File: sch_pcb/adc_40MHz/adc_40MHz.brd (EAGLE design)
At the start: 99 x 54.3 mm, 63 parts, among them IC1 LTC2227, IC2 LT6600-15, IC3 LTC6254XMS, IC5 LT1521XST, X1 SIGNAL, X2 CLK

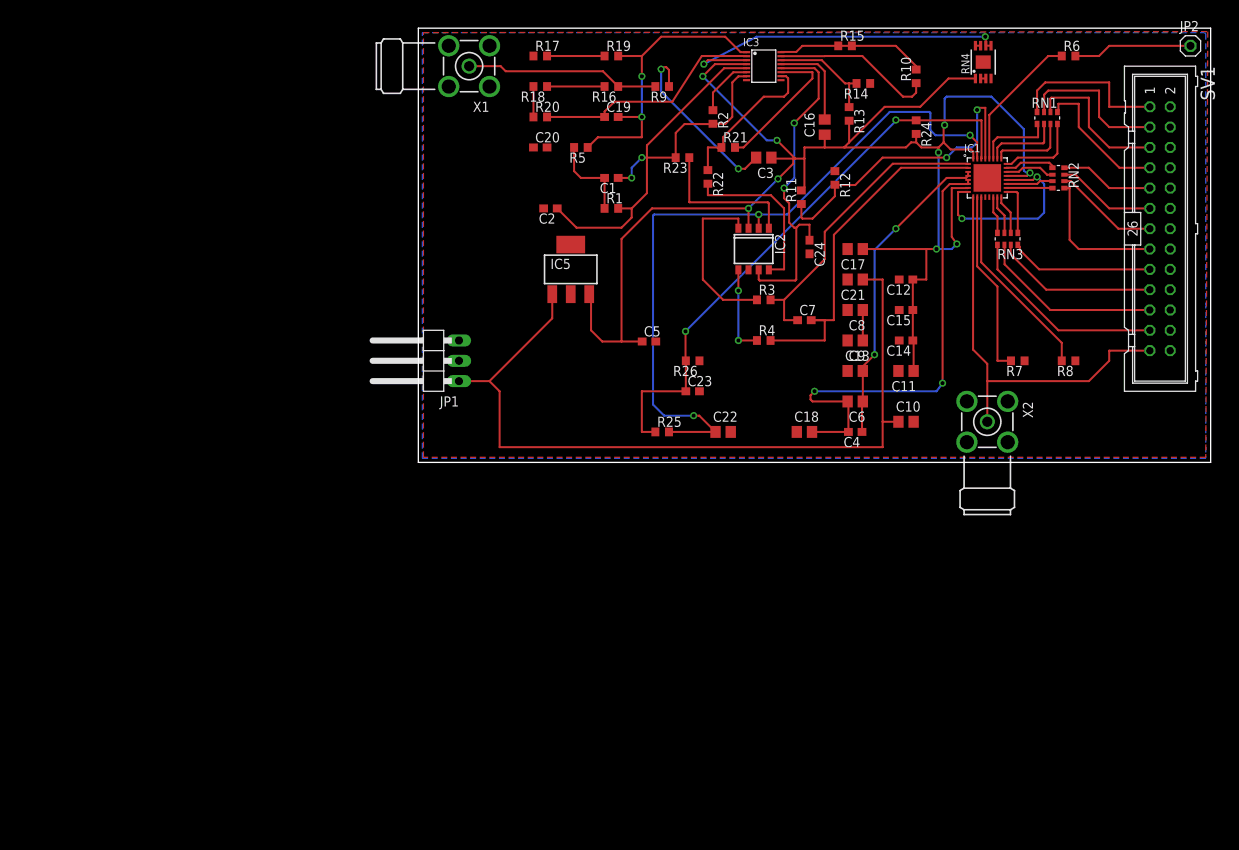
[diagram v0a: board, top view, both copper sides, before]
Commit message: Dokonczono model inwertera. Dodano go na schemat. Przed zmiana przetwornika na AD9235
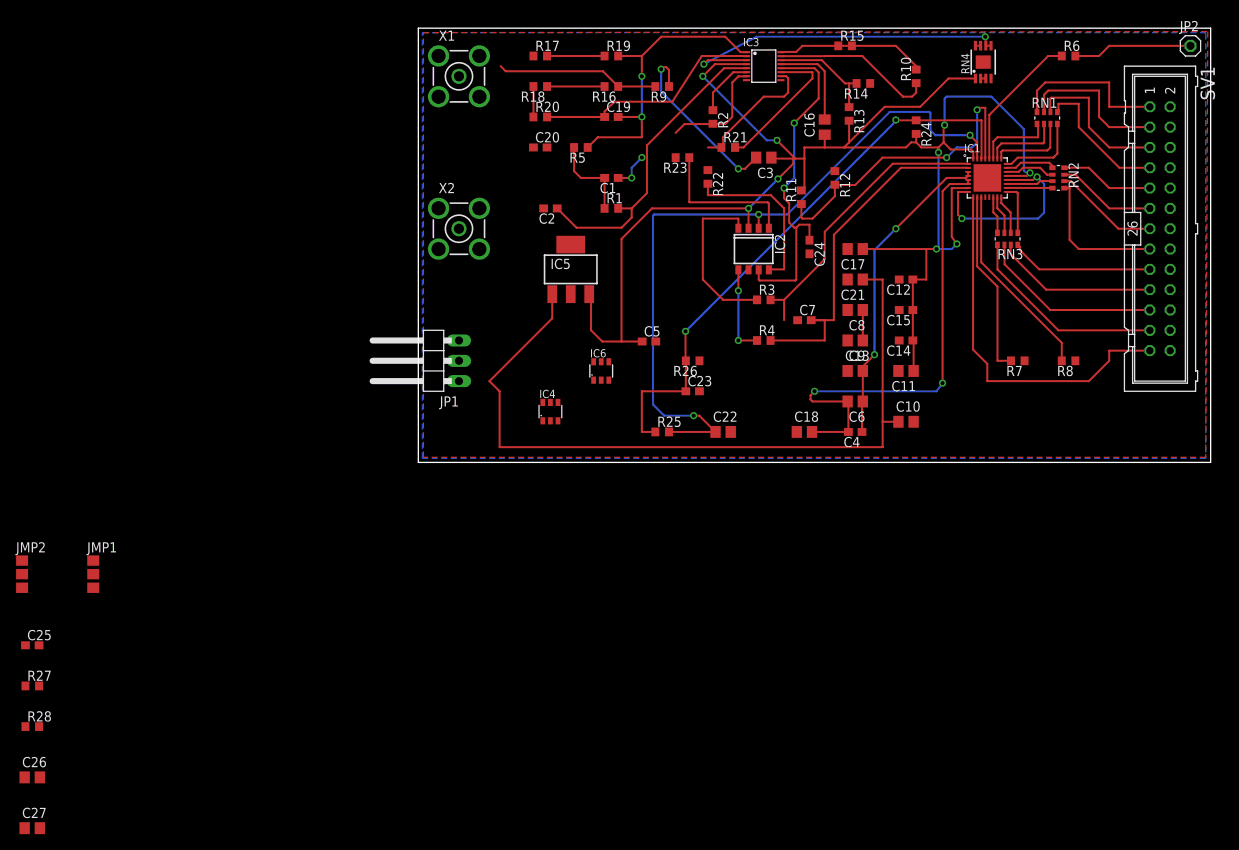
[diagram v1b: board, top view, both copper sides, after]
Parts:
- added C25: 51pF, rcl:C0603
- added C26, C27: 100n, rcl:C0805
- added IC4, IC6: SN74LVC2G14DBV, sn74lvc2g14:SOT23-6
- added JMP1, JMP2: 0R-JUMPA, jump-0r-smd:A0R-JMP
- added R27, R28: 0R, rcl:R0603
- X1: value SIGNAL -> BU-SMA-V; device con-coax:BU-SMA-H -> con-coax:BU-SMA-V
- X2: value CLK -> BU-SMA-V; device con-coax:BU-SMA-H -> con-coax:BU-SMA-V
- moved X2 70.3 mm to (5.08, 57.1), turned to 0 degrees
- moved X1 1.80 mm to (5.08, 76.2), turned to 0 degrees
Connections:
- new net N$34: IC4.1, X2.1
- new net N$36: IC4.3, IC4.6, JMP1.1
- new net N$37: IC1.9, IC6.1, JMP1.2
- new net N$38: IC6.3, IC6.6, JMP2.1
- new net N$39: IC4.4, JMP1.3
- new net N$40: R23.2, R28.1
- new net N$41: IC6.4, JMP2.3
- new net N$42: R22.1, R27.2
- net +3V3: now also C26.1, C27.1, IC4.5, IC6.5
- net CLK: now also JMP2.2; no longer IC1.9, X2.1
- net GND: now also C25.2, C26.2, C27.2, C7.1, IC4.2, IC6.2
- net N$13: now also R27.1; no longer R22.1
- net N$2: now also C25.1; no longer C7.1
- net N$27: now also R28.2; no longer R23.2
- net VIN: now also JP1.3; no longer JP1.1
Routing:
- net N$27: track 26.4 -> 19.1 mm
- net CLK: track 51.5 -> 46.4 mm
- net N$11: track 24.3 -> 20.4 mm
- net VIN: track 100.0 -> 96.2 mm
- net N$13: track 19.5 -> 16.3 mm
- net N$2: track 38.0 -> 36.3 mm

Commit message: Skończony (chyba) schemat dla nowego ADC i rozpoczęte układanie płytki
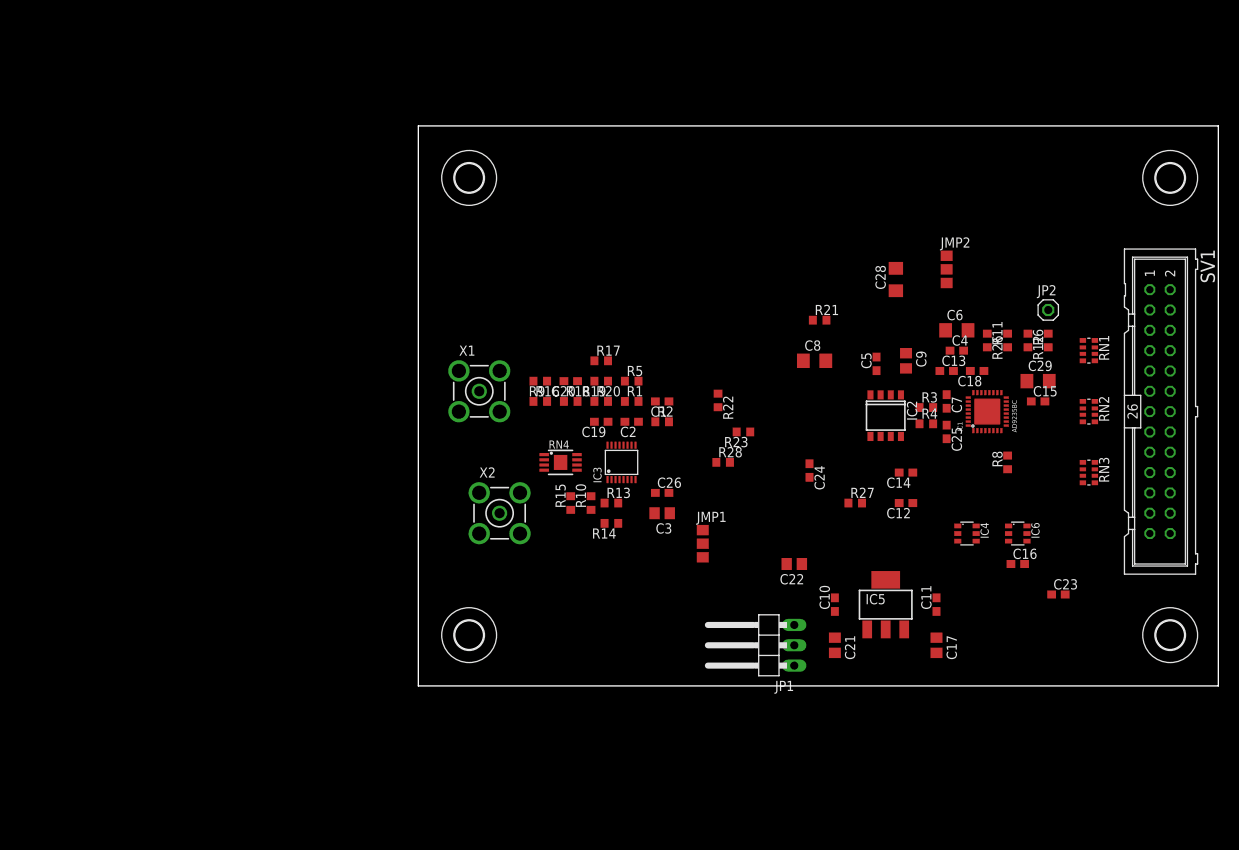
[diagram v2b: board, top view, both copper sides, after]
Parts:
- removed C27: 100n, rcl:C0805
- removed R24, R7: 0R, rcl:R0603
- removed R25: DNP, rcl:R0603
- added C28, C29: 10u, rcl:C1206
- added H1, H2, H3, H4: MOUNT-HOLE3.6, holes:3,6
- C10, C11, C16, C26: device rcl:C0805 -> rcl:C0603
- C13, C18: value 1u -> 100n; device rcl:C0805 -> rcl:C0603
- C22: value 2.2u -> 1u
- C24: value 51pF -> 100n
- C25, C7: value 51pF -> 51p
- C6, C8: value 2.2u -> 10u; device rcl:C0805 -> rcl:C1206
- IC1: value LTC2227 -> AD9235BC; device ltc22xx:QFN32 -> ad9235:LFCSP32
- R26: value DNP -> 0R
- X1: value BU-SMA-V -> Signal
- X2: value BU-SMA-V -> Clk
- moved JMP2 121.7 mm to (66.0, 52.1)
- moved C25 117.4 mm to (66.0, 31.8), turned to 270 degrees
- moved R27 105.4 mm to (54.6, 22.9)
- moved R28 92.5 mm to (38.1, 27.9)
- moved C26 86.4 mm to (30.5, 24.1)
- moved JMP1 76.3 mm to (35.6, 17.8)
- moved RN4 72.8 mm to (17.8, 27.9), turned to 270 degrees
- moved R10 67.1 mm to (21.6, 22.9)
- moved R15 66.6 mm to (19.1, 22.9), turned to 90 degrees
- moved R14 63.4 mm to (24.1, 20.3)
- moved C16 59.7 mm to (74.9, 15.2), turned to 0 degrees
- moved IC5 57.5 mm to (58.4, 10.2)
- moved R13 57.0 mm to (24.1, 22.9), turned to 0 degrees
- moved IC6 55.9 mm to (74.9, 19.1), turned to 270 degrees
- moved JP1 55.0 mm to (43.2, 5.08)
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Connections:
- removed net N$18: C24.1, IC2.7, IC3.12
- net +3V3: now also C23.1, C28.1, C29.1, IC1.16, IC1.27; no longer C14.1, C27.1, C8.1, IC1.21, IC1.7, R24.2
- net ADC_D0: now also IC1.7; no longer IC1.14
- net ADC_D1: now also IC1.8; no longer IC1.15
- net ADC_D10: now also IC1.19; no longer IC1.26
- net ADC_D11: now also IC1.20; no longer IC1.27
- net ADC_D2: now also IC1.9; no longer IC1.16
- net ADC_D3: now also IC1.10; no longer IC1.17
- net ADC_D4: now also IC1.11; no longer IC1.18
- net ADC_D5: now also IC1.12; no longer IC1.19
- net ADC_D6: now also IC1.13; no longer IC1.22
- net ADC_D7: now also IC1.14; no longer IC1.23
- net ADC_D8: now also IC1.17; no longer IC1.24
- net ADC_D9: now also IC1.18; no longer IC1.25
- net GND: now also C28.2, C29.2, IC1.15, IC1.28, IC1.31, IC1.EXP; no longer C27.2, IC1.20, IC1.33, IC1.8, R7.1
- net N$10: now also C22.1, C24.1, IC2.2, IC2.7, IC3.5; no longer IC1.10, R7.2
- net N$12: now also IC3.3; no longer IC3.14
- net N$13: now also IC3.7; no longer IC3.10
- net N$14: now also IC3.2; no longer IC3.15
- net N$15: now also IC3.1; no longer IC3.16
- net N$17: now also IC3.6; no longer IC3.11
- net N$2: now also IC1.29; no longer IC1.1
- net N$22: now also IC3.16; no longer IC3.1
- net N$23: now also IC3.15; no longer IC3.2
- net N$24: now also IC3.14; no longer IC3.3
- net N$26: now also IC3.11; no longer IC3.6
- net N$27: now also IC3.10; no longer IC3.7
- net N$29: now also IC3.12; no longer IC3.5
- net N$3: now also IC1.30; no longer IC1.2
- net N$32: now also IC1.22; no longer IC1.29
- net N$33: now also IC1.26; no longer IC1.3, IC1.4
- net N$35: now also IC1.23; no longer C23.1, IC1.30, R24.1, R25.1
- net N$37: now also IC1.2; no longer IC1.9
- net N$5: now also C14.1, C8.1, IC1.24; no longer C22.1, IC1.31, IC2.2, R25.2
- net N$6: now also IC1.21; no longer IC1.28
- net N$7: now also IC1.25; no longer IC1.5, IC1.6
- net N$9: now also IC1.4; no longer IC1.11
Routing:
- net +3V3: track 214.3 -> 0.00 mm, vias 9 -> 0
- net VIN: track 96.2 -> 0.00 mm
- net N$5: track 91.2 -> 0.00 mm, vias 3 -> 0
- net N$35: track 72.6 -> 0.00 mm, vias 2 -> 0
- net N$7: track 58.9 -> 0.00 mm, vias 2 -> 0
- net GND: track 58.6 -> 0.00 mm, vias 4 -> 0
- net CLK: track 46.4 -> 0.00 mm
- net N$3: track 44.8 -> 0.00 mm
- net N$24: track 43.4 -> 0.00 mm, vias 2 -> 0
- net N$18: track 43.2 -> 0.00 mm, vias 2 -> 0
- net N$32: track 40.1 -> 0.00 mm, vias 2 -> 0
- net N$33: track 39.4 -> 0.00 mm, vias 2 -> 0
- net N$29: track 38.8 -> 0.00 mm
- net N$22: track 38.3 -> 0.00 mm, vias 2 -> 0
- net N$2: track 36.3 -> 0.00 mm
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- removed copper zone on layer 1, net GND
- removed copper zone on layer 16, net GND
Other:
- board size 99 x 54.3 mm -> 100 x 70 mm

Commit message: Poprawiono biblioteki, tak żeby nie rzucały błędów DRC. Przy tworzeniu ścieżek wyłączyć warstwy tKeepout/bKeepout i włączyć tStop/bStop - kierować się tylko DRC
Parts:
- moved R2 3.81 mm to (27.4, 35.3)
- moved C1 3.30 mm to (27.4, 36.8)
- moved C2 3.23 mm to (24.4, 35.3)
- moved C19 2.75 mm to (21.3, 35.3)
- moved R1 2.62 mm to (24.4, 36.8), turned to 180 degrees
- moved R15 2.52 mm to (20.7, 24.8)
- moved R10 2.50 mm to (22.2, 25.3)
- moved R5 2.30 mm to (24.4, 38.4)
- moved IC3 2.09 mm to (24.9, 30.0)
- moved R20 1.98 mm to (21.3, 36.8)
- moved R17 1.70 mm to (21.3, 39.9)
- moved R19 1.55 mm to (21.3, 38.4)
- moved R18 1.48 mm to (18.3, 36.8)
- moved R16 1.27 mm to (15.2, 36.8)
- moved C20 0.80 mm to (18.3, 38.4)
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
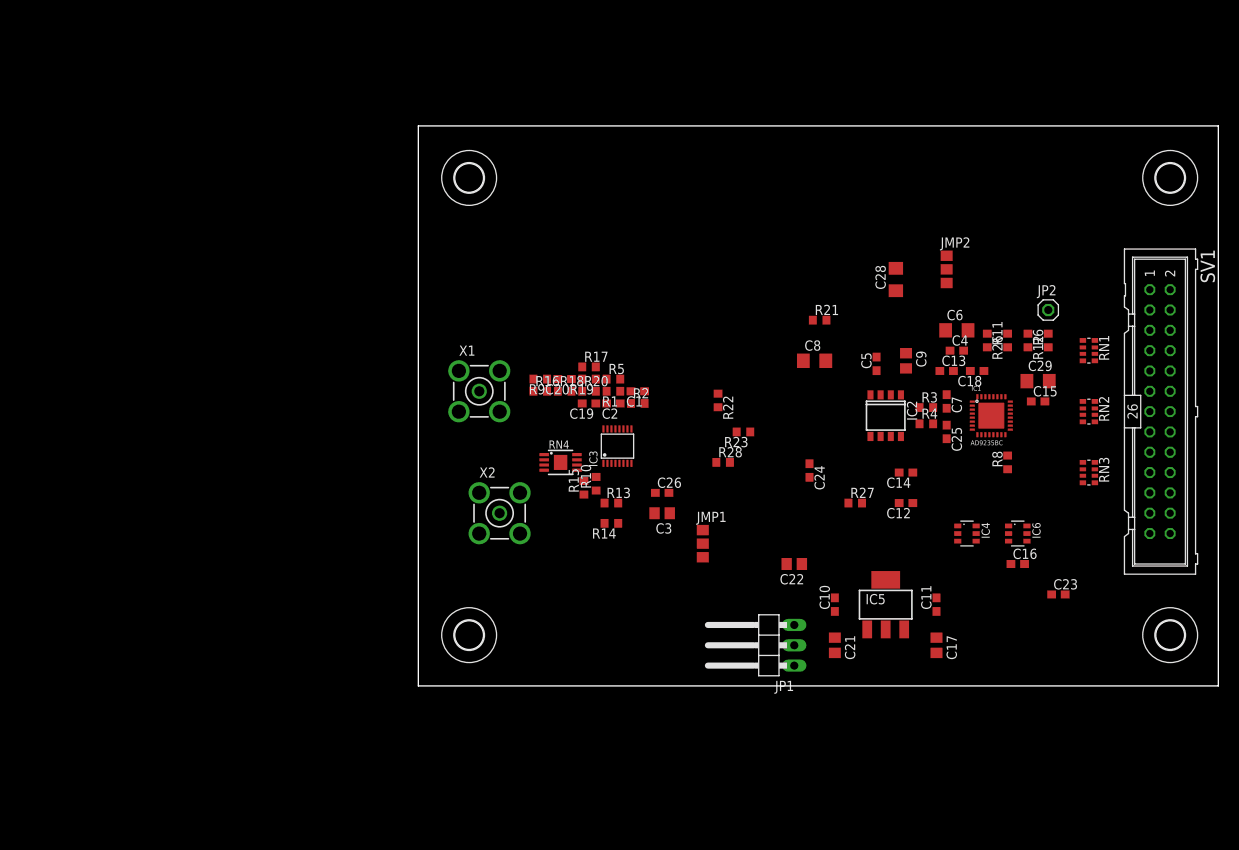
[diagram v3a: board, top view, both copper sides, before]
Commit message: Poprawiono kondensatory przy LT6600. Częściowe połączenie ścieżek (pierwsze stopnie filtru)
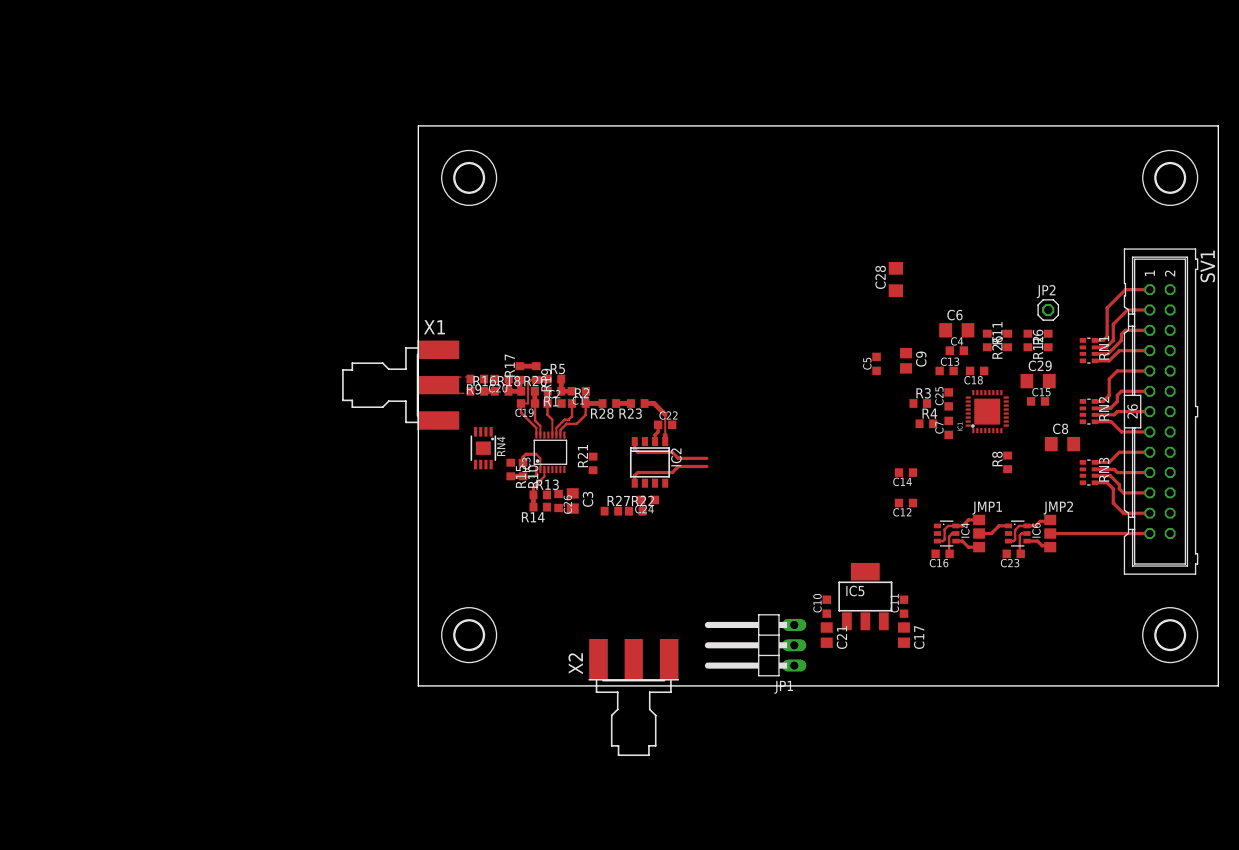
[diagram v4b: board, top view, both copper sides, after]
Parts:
- C1, C10, C11, C12, C13, C14, C15, C16, C18, C19, C2, C20, C23, C25, C26, C4, C5, C7: device rcl:C0603 -> resistor:C0603K
- C22: value 1u -> 10n; device rcl:C0805 -> resistor:C0603K
- C24: value 100n -> 10n; device rcl:C0603 -> resistor:C0603K
- X1: value Signal -> SMA-142-0701-851/861; device con-coax:BU-SMA-V -> con-coax:J502-ND-142-0701-851/861
- X2: value Clk -> SMA-142-0701-851/861; device con-coax:BU-SMA-V -> con-coax:J502-ND-142-0701-851/861
- moved JMP2 35.5 mm to (79.0, 19.1)
- moved JMP1 34.6 mm to (70.1, 19.1)
- moved R21 33.5 mm to (21.8, 27.8), turned to 90 degrees
- moved C8 32.7 mm to (80.5, 30.2)
- moved R27 30.5 mm to (24.1, 21.8)
- moved IC2 30.0 mm to (29.0, 27.9)
- moved X2 26.7 mm to (26.9, 0.76), turned to 90 degrees
- moved C22 23.7 mm to (30.9, 32.6), turned to 0 degrees
- moved C24 20.5 mm to (28.7, 23.2), turned to 180 degrees
- moved R22 17.2 mm to (27.2, 21.8), turned to 0 degrees
- moved R28 16.0 mm to (23.9, 35.3), turned to 180 degrees
- moved R23 13.7 mm to (27.4, 35.3)
- moved C26 13.0 mm to (17.5, 23.1), turned to 270 degrees
- moved C3 11.3 mm to (19.3, 23.1), turned to 270 degrees
- moved RN4 9.81 mm to (8.13, 29.7), turned to 180 degrees
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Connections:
- removed net N$11: R16.1, R9.2, X1.1
- net GND: now also X1.G@1, X1.G@2, X1.G@3, X1.G@4, X2.G@1, X2.G@2, X2.G@3, X2.G@4; no longer X1.2, X1.3, X1.4, X1.5, X2.2, X2.3, X2.4, X2.5
- net VIN: now also R16.1, R9.2, X1.1
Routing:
- net CLK: track 0.00 -> 12.4 mm
- net DAC_D11: track 0.00 -> 11.6 mm
- net N$22: track 0.00 -> 10.8 mm
- net N$4: track 0.00 -> 10.4 mm
- net N$1: track 0.00 -> 10.4 mm
- net DAC_D10: track 0.00 -> 10.00 mm
- net N$27: track 0.00 -> 9.64 mm
- net DAC_D7: track 0.00 -> 9.64 mm
- net DAC_D0: track 0.00 -> 9.49 mm
- net DAC_D9: track 0.00 -> 8.53 mm
- net DAC_D6: track 0.00 -> 8.20 mm
- net DAC_D1: track 0.00 -> 8.05 mm
- net DAC_D8: track 0.00 -> 7.40 mm
- net DAC_D4: track 0.00 -> 7.39 mm
- net DAC_D3: track 0.00 -> 7.39 mm
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- added copper zone on layer 1, net VIN
